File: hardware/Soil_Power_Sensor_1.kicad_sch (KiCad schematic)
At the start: 24 parts, among them J1 Voltage, J2 Current, J3 GND, J4 Rsense, J7 PinJumper_02x03, U1 THS4532, U2 MAX9944, U3 INA296A, U4 ADS1219

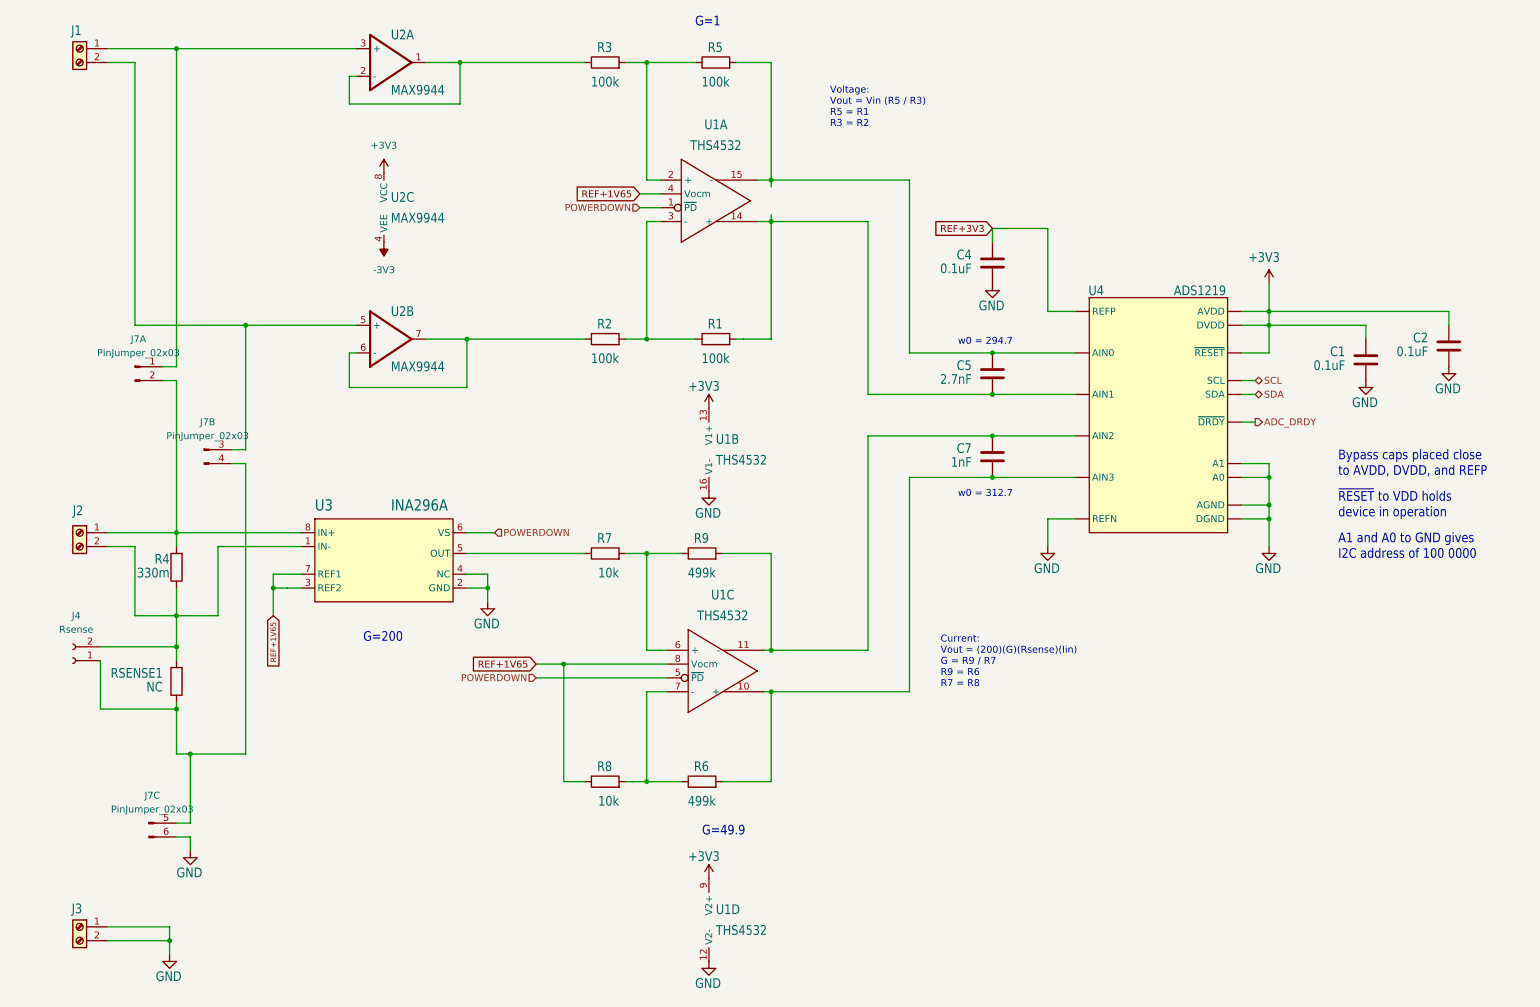
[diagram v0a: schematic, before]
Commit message: Adding general improvements to sensor PCB
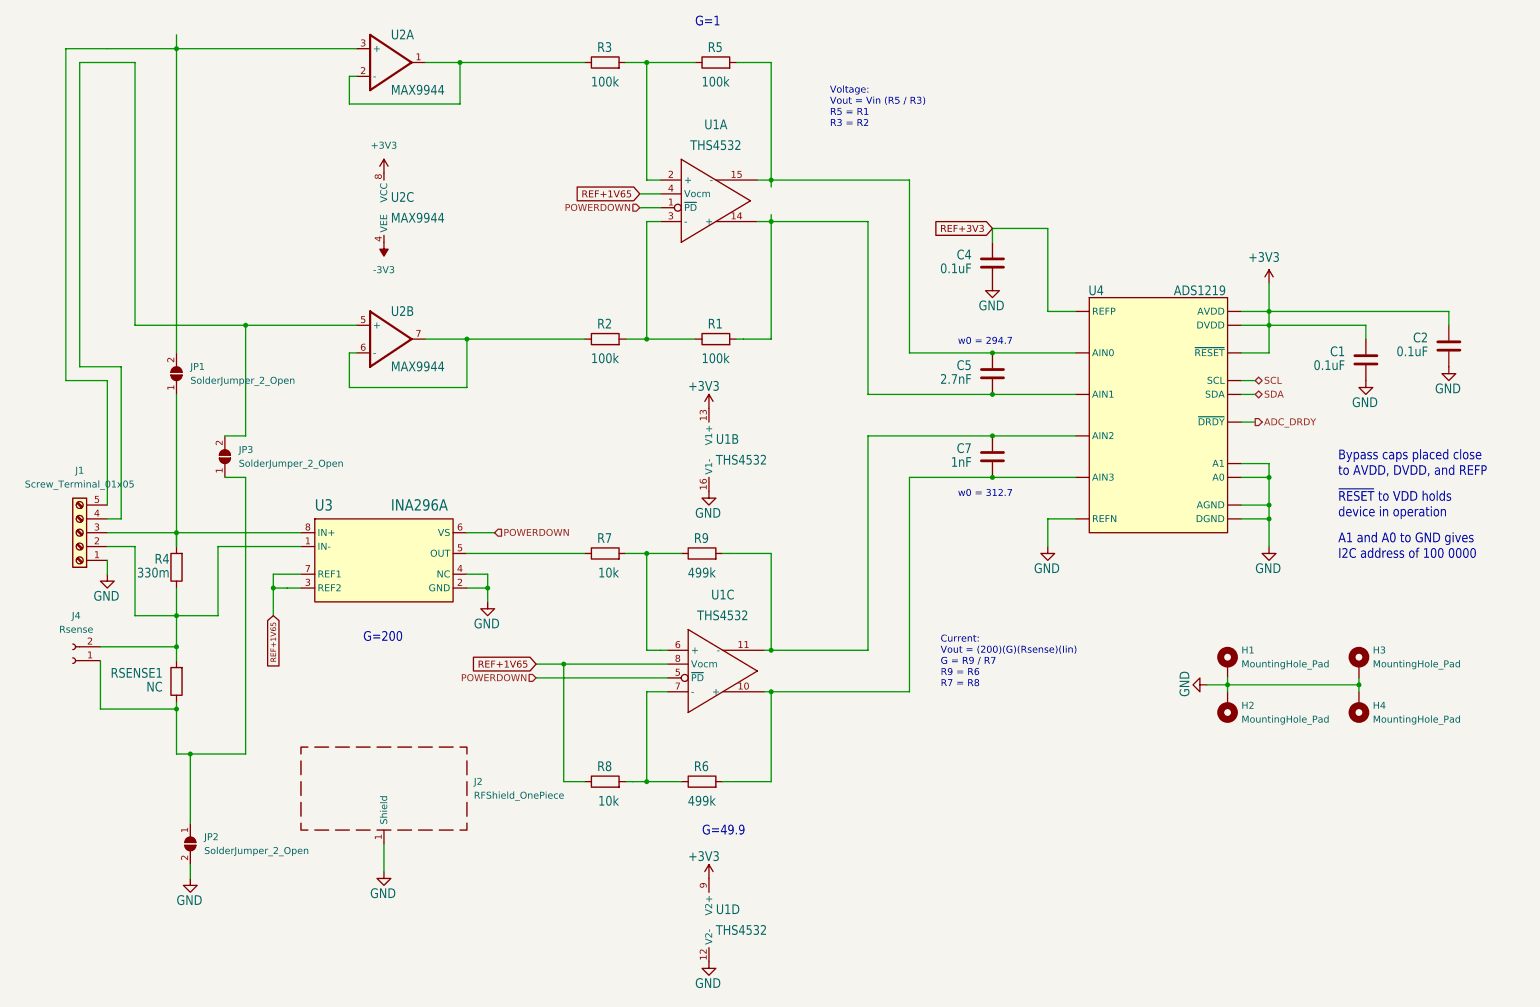
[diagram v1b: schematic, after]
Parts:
- removed J1: Voltage, TerminalBlock_WAGO:TerminalBlock_WAGO_236-102_1x02_P5.00mm_45Degree, symbol Connector:Screw_Terminal_01x02
- removed J2: Current, TerminalBlock_WAGO:TerminalBlock_WAGO_236-102_1x02_P5.00mm_45Degree, symbol Connector:Screw_Terminal_01x02
- removed J3: GND, TerminalBlock_WAGO:TerminalBlock_WAGO_236-102_1x02_P5.00mm_45Degree, symbol Connector:Screw_Terminal_01x02
- removed J7: PinJumper_02x03, Connector_PinHeader_2.54mm:PinHeader_2x03_P2.54mm_Vertical, symbol Soil Power Sensor-eagle-import:PinJumper_02x03
- added H1, H2, H3, H4: MountingHole_Pad, MountingHole:MountingHole_3.2mm_M3_ISO7380_Pad_TopBottom, symbol Mechanical:MountingHole_Pad
- added J1: Screw_Terminal_01x05, TerminalBlock_WAGO:TerminalBlock_WAGO_236-205_1x05_P7.50mm_45Degree, symbol Connector:Screw_Terminal_01x05
- added J2: RFShield_OnePiece, RF_Shielding:Wuerth_36103305_30x30mm, symbol Device:RFShield_OnePiece
- added JP1, JP2, JP3: SolderJumper_2_Open, Jumper:SolderJumper-2_P1.3mm_Open_RoundedPad1.0x1.5mm, symbol Jumper:SolderJumper_2_Open
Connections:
- net GND: now also H1.1, H2.1, H3.1, H4.1, J1.1 (Pin_1), J2.1 (Shield), JP2.2 (B)
- net at R4.2, U3.8 (IN+): now also J1.3 (Pin_3), JP1.1 (A)
- net at J4.2 (Pin_2), R4.1, RSENSE1.2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: now also J1.2 (Pin_2)
- net at J4.1 (Pin_1), RSENSE1.1: now also JP2.1 (A), JP3.1 (A)
- net at U2.3 (+): now also J1.5 (Pin_5), JP1.2 (B)
- net at U2.5 (+): now also J1.4 (Pin_4), JP3.2 (B)

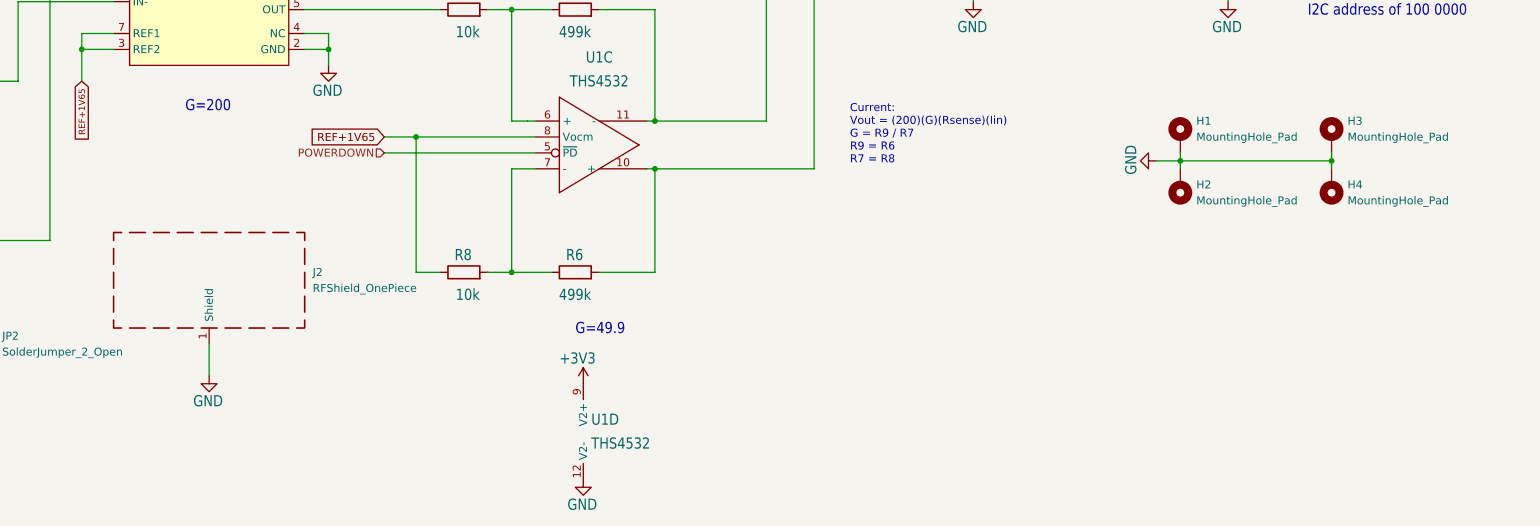
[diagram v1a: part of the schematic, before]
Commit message: Moved hardware components to new sheet
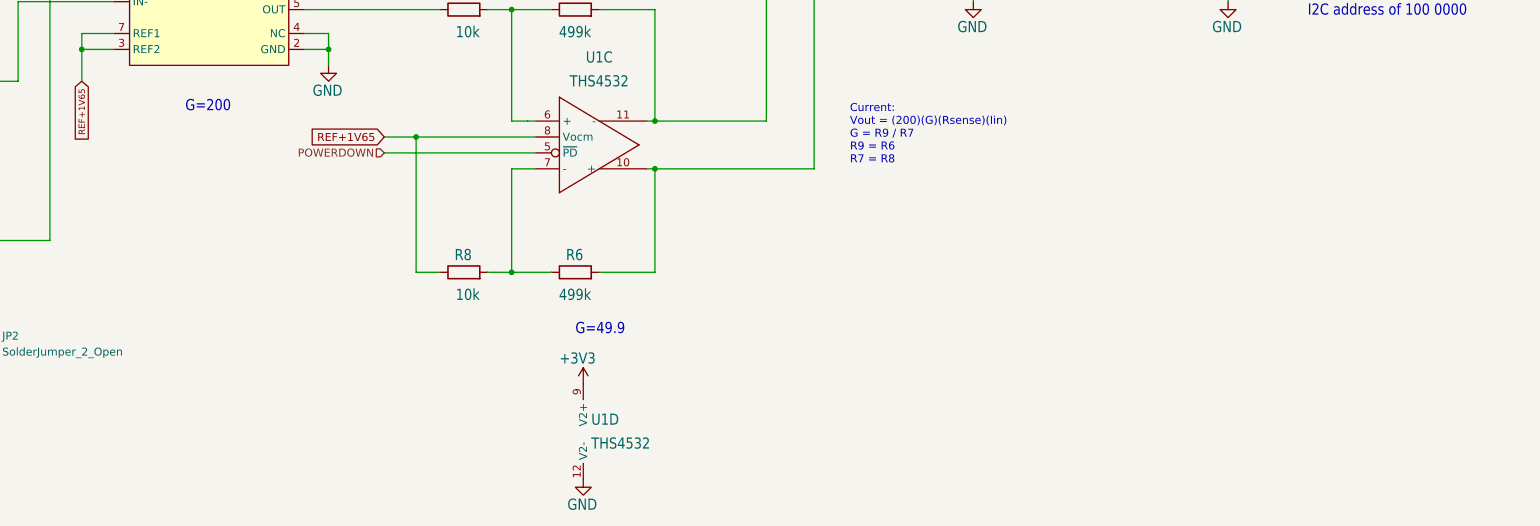
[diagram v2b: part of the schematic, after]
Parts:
- removed H1, H2, H3, H4: MountingHole_Pad, MountingHole:MountingHole_3.2mm_M3_ISO7380_Pad_TopBottom, symbol Mechanical:MountingHole_Pad
- removed J2: RFShield_OnePiece, RF_Shielding:Wuerth_36103305_30x30mm, symbol Device:RFShield_OnePiece
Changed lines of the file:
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@@
   (junction (at 236.22 99.06) (diameter 0) (color 0 0 0 0)
   )
-  (junction (at 228.6 137.16) (diameter 0) (color 0 0 0 0)
-  )
   (junction (at 144.78 130.81) (diameter 0) (color 0 0 0 0)
   )
@@
   (junction (at 236.22 71.12) (diameter 0) (color 0 0 0 0)
   )
-  (junction (at 252.73 137.16) (diameter 0) (color 0 0 0 0)
-  )
   (junction (at 121.92 154.94) (diameter 0) (color 0 0 0 0)
   )
@@
     (stroke (width 0.1524) (type solid))
   )
-  (wire (pts (xy 228.6 135.89) (xy 228.6 137.16))
-    (stroke (width 0) (type default))
-  )
   (wire (pts (xy 88.9 82.55) (xy 88.9 73.66))
     (stroke (width 0.1524) (type solid))
@@
     (stroke (width 0.1524) (type solid))
   )
-  (wire (pts (xy 252.73 135.89) (xy 252.73 137.16))
-    (stroke (width 0) (type default))
-  )
   (wire (pts (xy 88.9 109.22) (xy 93.98 109.22))
     (stroke (width 0.1524) (type solid))
@@
     (stroke (width 0.1524) (type solid))
   )
-  (wire (pts (xy 228.6 137.16) (xy 252.73 137.16))
-    (stroke (width 0) (type default))
-  )
   (wire (pts (xy 68.58 76.2) (xy 67.31 76.2))
     (stroke (width 0.1524) (type solid))
@@
     (stroke (width 0) (type default))
   )
-  (wire (pts (xy 224.79 137.16) (xy 228.6 137.16))
-    (stroke (width 0) (type default))
-  )
   (wire (pts (xy 38.1 149.86) (xy 35.56 149.86))
     (stroke (width 0.1524) (type solid))
@@
     (stroke (width 0) (type default))
   )
-  (wire (pts (xy 228.6 137.16) (xy 228.6 138.43))
-    (stroke (width 0) (type default))
-  )
   (wire (pts (xy 185.42 76.2) (xy 200.66 76.2))
     (stroke (width 0.1524) (type solid))
@@
     (stroke (width 0.1524) (type solid))
   )
-  (wire (pts (xy 252.73 137.16) (xy 252.73 138.43))
-    (stroke (width 0) (type default))
-  )
   (wire (pts (xy 35.56 20.32) (xy 22.86 20.32))
     (stroke (width 0.1524) (type solid))
@@
   (wire (pts (xy 144.78 73.66) (xy 144.78 52.07))
     (stroke (width 0.1524) (type solid))
-  )
-  (wire (pts (xy 73.66 166.37) (xy 73.66 171.45))
-    (stroke (width 0) (type default))
   )
   (wire (pts (xy 21.59 132.715) (xy 21.59 141.605))
@@
     )
   )
-  (symbol (lib_id "Mechanical:MountingHole_Pad") (at 252.73 140.97 180) (unit 1)
-    (in_bom yes) (on_board yes) (dnp no) (fields_autoplaced)
-    (property "Reference" "H4" (at 255.27 140.97 0)
-      (effects (font (size 1.27 1.27)) (justify right))
-    )
-    (property "Value" "MountingHole_Pad" (at 255.27 143.51 0)
-      (effects (font (size 1.27 1.27)) (justify right))
-    )
-    (property "Footprint" "MountingHole:MountingHole_3.2mm_M3_ISO7380_Pad_TopBottom" (at 252.73 140.97 0)
-      (effects (font (size 1.27 1.27)) hide)
-    )
-    (property "Datasheet" "~" (at 252.73 140.97 0)
-      (effects (font (size 1.27 1.27)) hide)
-    )
-    (pin "1")
-    (instances
-      (project "Soil Power Sensor"
-        (path "/5300ec4d-4648-40a1-8d89-4fa6b3bf32a3/643deee0-b2c1-47dd-8bbd-6697ae8f1315"
-          (reference "H4") (unit 1)
-        )
-      )
-    )
-  )
   (symbol (lib_id "power:GND") (at 133.35 187.96 0) (unit 1)
     (in_bom yes) (on_board yes) (dnp no)
@@
     )
   )
-  (symbol (lib_id "Device:RFShield_OnePiece") (at 73.66 156.21 0) (unit 1)
-    (in_bom yes) (on_board yes) (dnp no) (fields_autoplaced)
-    (property "Reference" "J2" (at 90.17 154.94 0)
-      (effects (font (size 1.27 1.27)) (justify left))
-    )
-    (property "Value" "RFShield_OnePiece" (at 90.17 157.48 0)
-      (effects (font (size 1.27 1.27)) (justify left))
-    )
-    (property "Footprint" "RF_Shielding:Wuerth_36103305_30x30mm" (at 73.66 158.75 0)
-      (effects (font (size 1.27 1.27)) hide)
-    )
-    (property "Datasheet" "~" (at 73.66 158.75 0)
-      (effects (font (size 1.27 1.27)) hide)
-    )
-    (pin "1")
-    (instances
-      (project "Soil Power Sensor"
-        (path "/5300ec4d-4648-40a1-8d89-4fa6b3bf32a3/643deee0-b2c1-47dd-8bbd-6697ae8f1315"
-          (reference "J2") (unit 1)
-        )
-      )
-    )
-  )
-  (symbol (lib_id "Mechanical:MountingHole_Pad") (at 228.6 140.97 180) (unit 1)
-    (in_bom yes) (on_board yes) (dnp no) (fields_autoplaced)
-    (property "Reference" "H2" (at 231.14 140.97 0)
-      (effects (font (size 1.27 1.27)) (justify right))
-    )
-    (property "Value" "MountingHole_Pad" (at 231.14 143.51 0)
-      (effects (font (size 1.27 1.27)) (justify right))
-    )
-    (property "Footprint" "MountingHole:MountingHole_3.2mm_M3_ISO7380_Pad_TopBottom" (at 228.6 140.97 0)
-      (effects (font (size 1.27 1.27)) hide)
-    )
-    (property "Datasheet" "~" (at 228.6 140.97 0)
-      (effects (font (size 1.27 1.27)) hide)
-    )
-    (pin "1")
-    (instances
-      (project "Soil Power Sensor"
-        (path "/5300ec4d-4648-40a1-8d89-4fa6b3bf32a3/643deee0-b2c1-47dd-8bbd-6697ae8f1315"
-          (reference "H2") (unit 1)
-        )
-      )
-    )
-  )
   (symbol (lib_id "Device:C") (at 185.42 59.69 0) (unit 1)
     (in_bom yes) (on_board yes) (dnp no)
@@
         )
       )
-    )
-  )
-  (symbol (lib_id "power:GND") (at 224.79 137.16 270) (unit 1)
-    (in_bom yes) (on_board yes) (dnp no)
-    (property "Reference" "#GND025" (at 224.79 137.16 0)
-      (effects (font (size 1.27 1.27)) hide)
-    )
-    (property "Value" "GND" (at 219.71 134.62 0)
-      (effects (font (size 1.778 1.5113)) (justify left bottom))
-    )
-    (property "Footprint" "" (at 224.79 137.16 0)
-      (effects (font (size 1.27 1.27)) hide)
-    )
-    (property "Datasheet" "" (at 224.79 137.16 0)
-      (effects (font (size 1.27 1.27)) hide)
-    )
-    (pin "1")
-    (instances
-      (project "Soil Power Sensor"
-        (path "/5300ec4d-4648-40a1-8d89-4fa6b3bf32a3/643deee0-b2c1-47dd-8bbd-6697ae8f1315"
-          (reference "#GND025") (unit 1)
-        )
-      )
-    )
-  )
-  (symbol (lib_id "power:GND") (at 73.66 171.45 0) (unit 1)
-    (in_bom yes) (on_board yes) (dnp no)
-    (property "Reference" "#GND01" (at 73.66 171.45 0)
-      (effects (font (size 1.27 1.27)) hide)
-    )
-    (property "Value" "GND" (at 71.12 176.53 0)
-      (effects (font (size 1.778 1.5113)) (justify left bottom))
-    )
-    (property "Footprint" "" (at 73.66 171.45 0)
-      (effects (font (size 1.27 1.27)) hide)
-    )
-    (property "Datasheet" "" (at 73.66 171.45 0)
-      (effects (font (size 1.27 1.27)) hide)
-    )
-    (pin "1")
-    (instances
-      (project "Soil Power Sensor"
-        (path "/5300ec4d-4648-40a1-8d89-4fa6b3bf32a3/643deee0-b2c1-47dd-8bbd-6697ae8f1315"
-          (reference "#GND01") (unit 1)
-        )
-      )
-    )
-  )
-  (symbol (lib_id "Mechanical:MountingHole_Pad") (at 252.73 133.35 0) (unit 1)
-    (in_bom yes) (on_board yes) (dnp no) (fields_autoplaced)
-    (property "Reference" "H3" (at 255.27 130.81 0)
-      (effects (font (size 1.27 1.27)) (justify left))
-    )
-    (property "Value" "MountingHole_Pad" (at 255.27 133.35 0)
-      (effects (font (size 1.27 1.27)) (justify left))
-    )
-    (property "Footprint" "MountingHole:MountingHole_3.2mm_M3_ISO7380_Pad_TopBottom" (at 252.73 133.35 0)
-      (effects (font (size 1.27 1.27)) hide)
-    )
-    (property "Datasheet" "~" (at 252.73 133.35 0)
-      (effects (font (size 1.27 1.27)) hide)
-    )
-    (pin "1")
-    (instances
-      (project "Soil Power Sensor"
-        (path "/5300ec4d-4648-40a1-8d89-4fa6b3bf32a3/643deee0-b2c1-47dd-8bbd-6697ae8f1315"
-          (reference "H3") (unit 1)
-        )
-      )
-    )
-  )
-  (symbol (lib_id "Mechanical:MountingHole_Pad") (at 228.6 133.35 0) (unit 1)
-    (in_bom yes) (on_board yes) (dnp no) (fields_autoplaced)
-    (property "Reference" "H1" (at 231.14 130.81 0)
-      (effects (font (size 1.27 1.27)) (justify left))
-    )
-    (property "Value" "MountingHole_Pad" (at 231.14 133.35 0)
-      (effects (font (size 1.27 1.27)) (justify left))
-    )
-    (property "Footprint" "MountingHole:MountingHole_3.2mm_M3_ISO7380_Pad_TopBottom" (at 228.6 133.35 0)
-      (effects (font (size 1.27 1.27)) hide)
-    )
-    (property "Datasheet" "~" (at 228.6 133.35 0)
-      (effects (font (size 1.27 1.27)) hide)
-    )
-    (pin "1")
-    (instances
-      (project "Soil Power Sensor"
-        (path "/5300ec4d-4648-40a1-8d89-4fa6b3bf32a3/643deee0-b2c1-47dd-8bbd-6697ae8f1315"
-          (reference "H1") (unit 1)
-        )
-      )
